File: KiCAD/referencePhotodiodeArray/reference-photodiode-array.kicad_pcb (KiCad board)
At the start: 2 copper layers, 28 x 28 mm, 29 parts

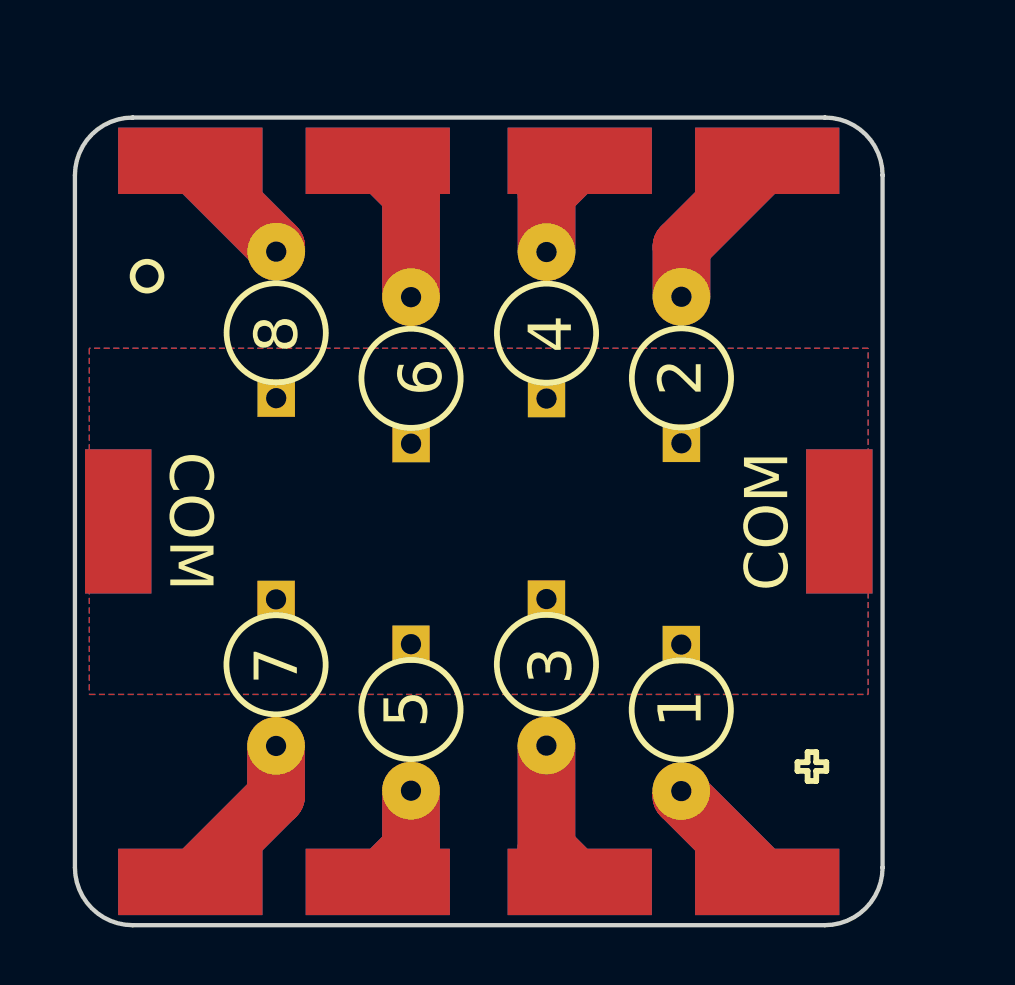
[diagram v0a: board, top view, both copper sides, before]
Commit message: made new photodiode array, fixed springpin board
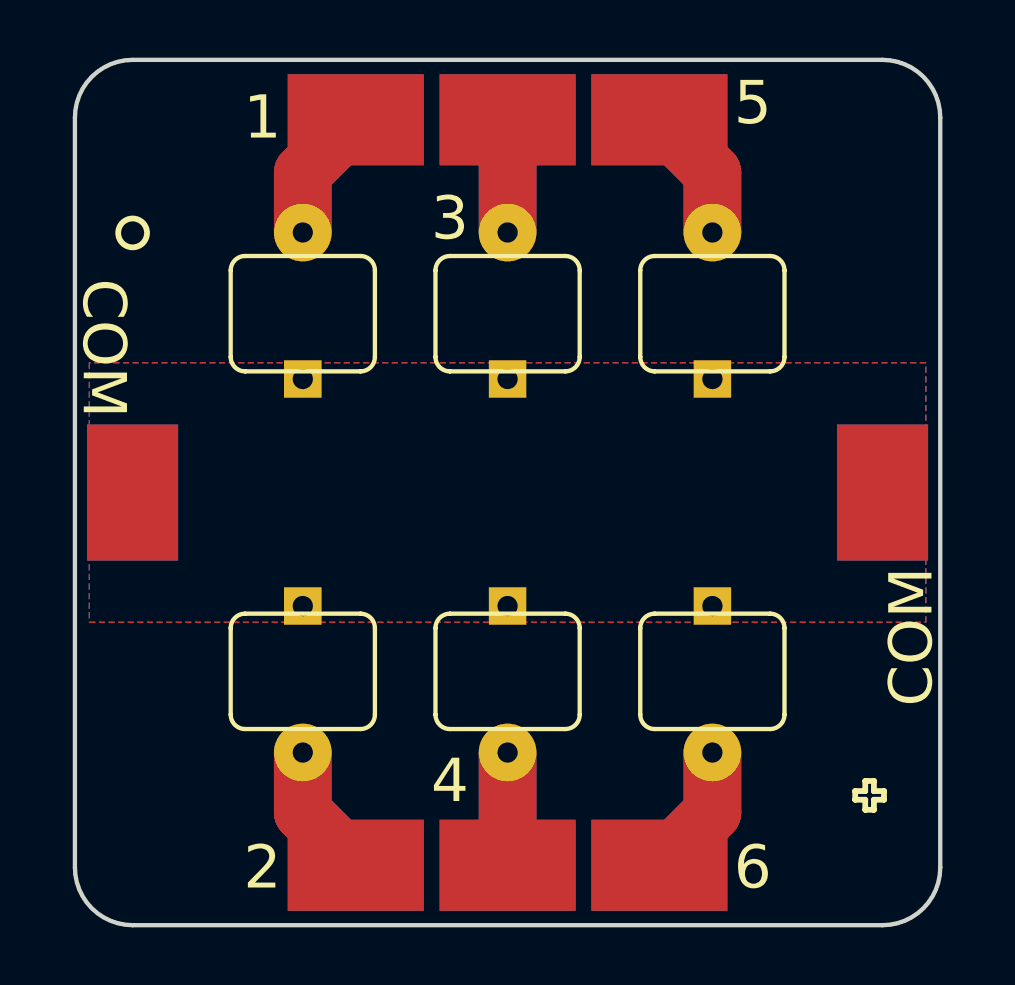
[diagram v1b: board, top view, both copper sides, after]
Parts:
- removed D7, D8: D_Photo, testPad:BPW34
- removed the G*** at (14.0, -14.0)
- removed W18, W19, W8, W9: TEST_1P, testPad:SolderWirePad_single_SMD_5x2.3mm
- added G***: value, myParts:logo_small, B.Cu at (15.0, -15.0)
- D1, D2, D3, D4, D5, D6: footprint testPad:BPW34 -> myParts:BPW34
- W1, W10, W11, W12, W13, W14, W15, W16, W17, W2, W20, W3, W4, W5, W6, W7: footprint testPad:SolderWirePad_single_SMD_5x2.3mm -> myParts:SolderWirePad_single_SMD_4.7x3.2mm
- moved W12 5.91 mm to (9.74, -27.9)
- moved W2 5.91 mm to (9.74, -27.9)
- moved D5 5.79 mm to (22.1, -18.9)
- moved W13 5.77 mm to (9.74, -2.08)
- moved W3 5.77 mm to (9.74, -2.08)
- moved D6 5.76 mm to (22.1, -11.1)
- moved W14 4.72 mm to (15.0, -27.9)
- moved W4 4.72 mm to (15.0, -27.9)
- moved W15 4.54 mm to (15.0, -2.08)
- moved W5 4.54 mm to (15.0, -2.08)
- moved D3 4.03 mm to (15.0, -18.9)
- moved D4 3.60 mm to (15.0, -11.1)
- moved W16 3.11 mm to (20.3, -27.9)
- moved W6 3.11 mm to (20.3, -27.9)
- moved W17 2.82 mm to (20.3, -2.08)
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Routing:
- net Net-(D7-Pad2): track 11.9 -> 0.00 mm
- net Net-(D8-Pad2): track 8.76 -> 0.00 mm
- net Net-(D3-Pad2): track 10.4 -> 7.82 mm
- net Net-(D2-Pad2): track 11.9 -> 9.34 mm
- net Net-(D5-Pad2): track 7.28 -> 9.34 mm
- net Net-(D6-Pad2): track 10.4 -> 9.34 mm
- net Net-(D1-Pad2): track 8.76 -> 9.34 mm
- net Net-(D4-Pad2): track 7.28 -> 7.81 mm
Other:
- board size 28 x 28 mm -> 30 x 30 mm
- board text removed: "7"
- board text removed: "8"

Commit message: generate order packages
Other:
- board text added: "17e0726"
- board text removed: "v1.01"
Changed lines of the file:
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@@
     (pcbplotparams
       (layerselection 0x010fc_ffffffff)
-      (usegerberextensions false)
+      (usegerberextensions true)
       (usegerberattributes true)
       (excludeedgelayer true)
@@
     (effects (font (size 1.5 1.5) (thickness 0.3)))
   )
-  (gr_text v1.01 (at 24 -16 180) (layer B.SilkS)
+  (gr_text 17e0726 (at 24 -16 180) (layer B.SilkS)
     (effects (font (size 0.5 0.5) (thickness 0.125)) (justify mirror))
   )
